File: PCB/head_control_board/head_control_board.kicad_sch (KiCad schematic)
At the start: 60 parts, among them Q1 AO3401A, U1 TPS63070RNMR, U2 TPS63070RNMR, U3 SN74AHCT245PWR, U4 ESP32-S3-WROOM-1(N16R8)

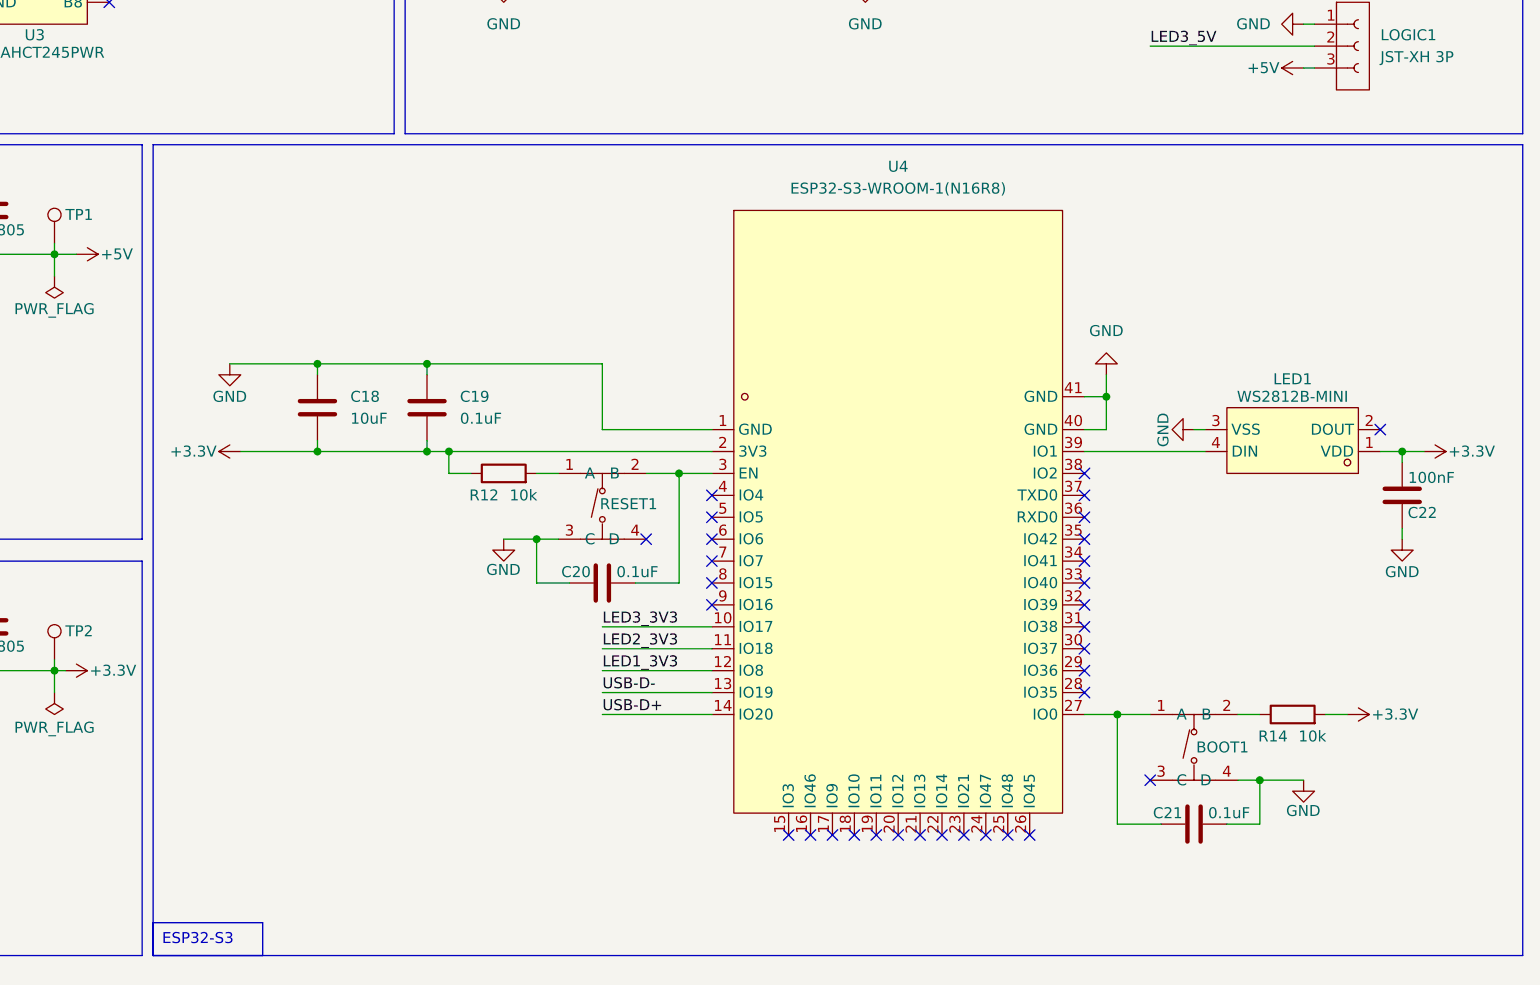
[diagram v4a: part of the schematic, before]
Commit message: Finish signal routing
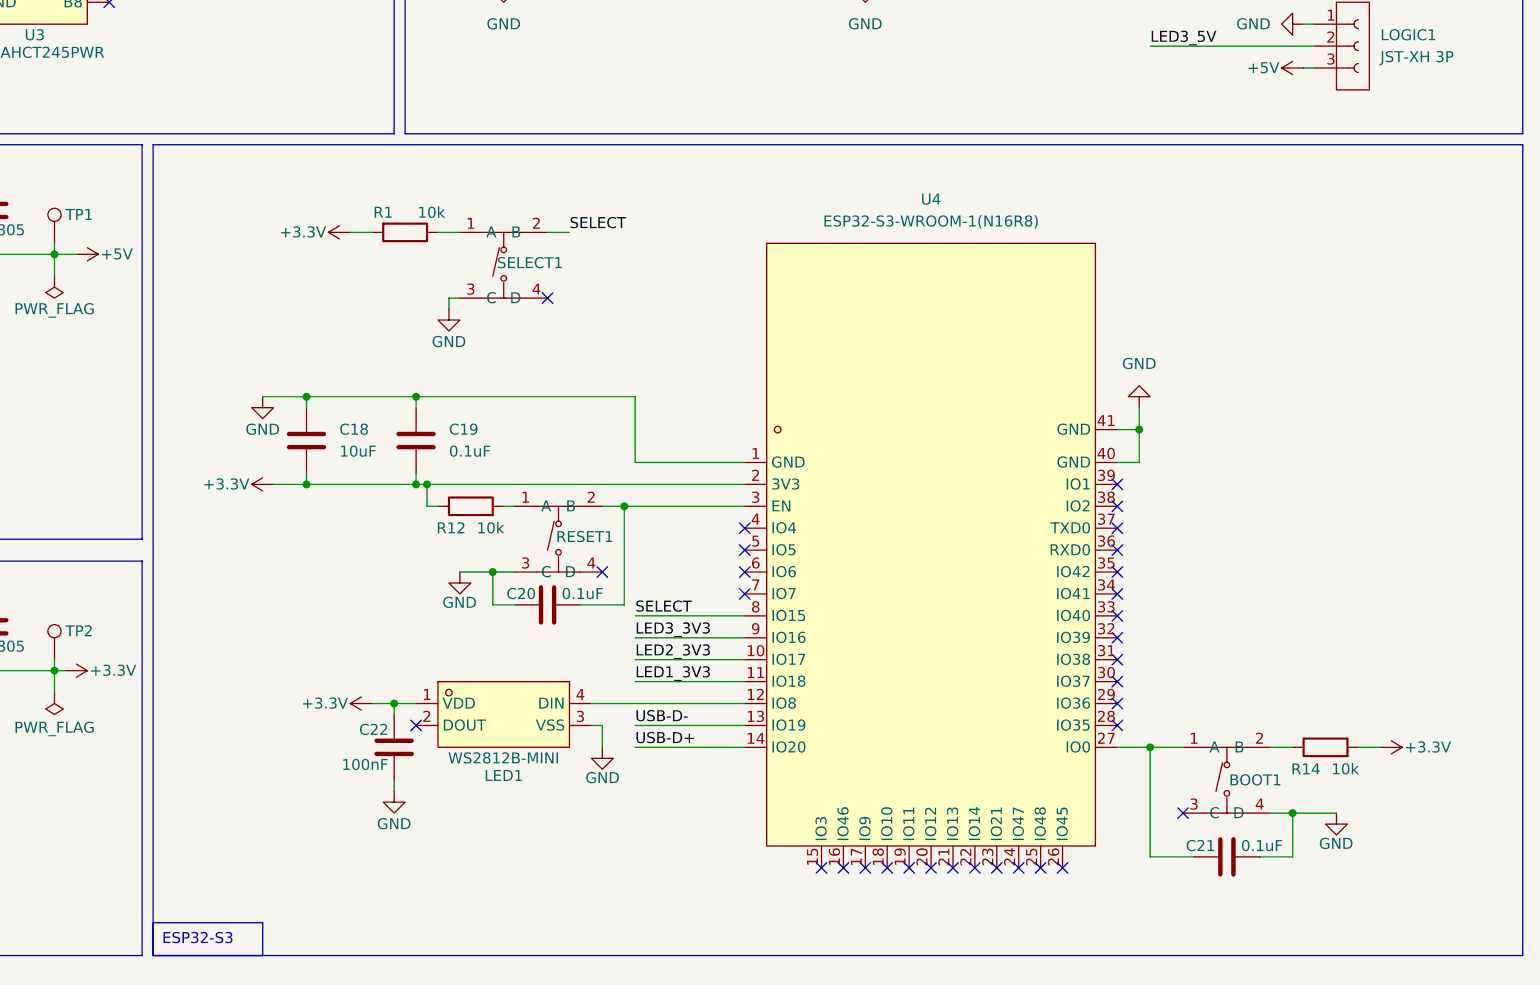
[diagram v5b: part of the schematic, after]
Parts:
- added R1: 10k, Resistor_SMD:R_0805_2012Metric, symbol Device:R
- added SELECT1: TS-1187A-B-A-B, LCSC:SW-SMD_4P-L5.1-W5.1-P3.70-LS6.5-TL-2, symbol LCSC:TS-1187A-B-A-B
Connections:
- net +3.3V: now also C22.1, R1.2; no longer C22.2
- net GND: now also C22.2, SELECT1.3 (C); no longer C22.1
- net LED1_3V3: now also U4.11 (IO18); no longer U4.12 (IO8)
- net LED2_3V3: now also U4.10 (IO17); no longer U4.11 (IO18)
- net LED3_3V3: now also U4.9 (IO16); no longer U4.10 (IO17)
- net at LED1.4 (DIN): now also U4.12 (IO8); no longer U4.39 (IO1)
- net SELECT: now reaches U4.8 (IO15)
- net SELECT: now also SELECT1.2 (B)
- new net: R1.1, SELECT1.1 (A)
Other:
- moved on the sheet: BOOT1, C18, C19, C20, C21, C22, LED1, R12, R14, RESET1, U4

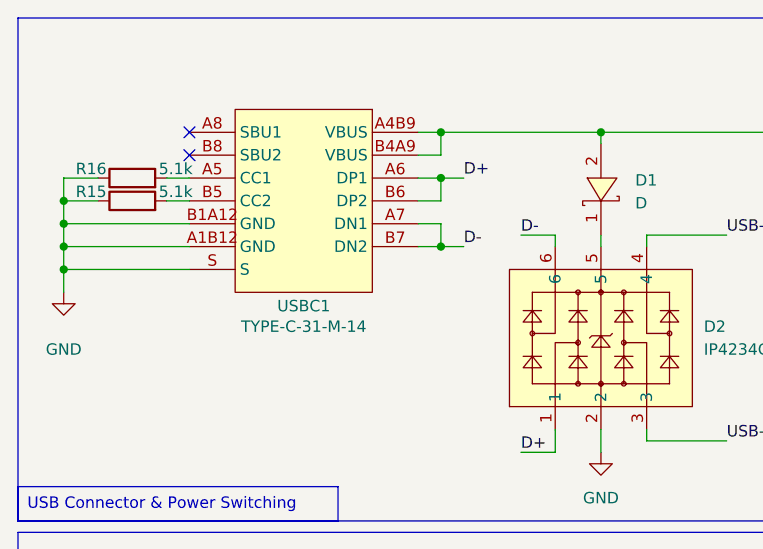
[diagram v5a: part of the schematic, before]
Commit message: Finish power routing
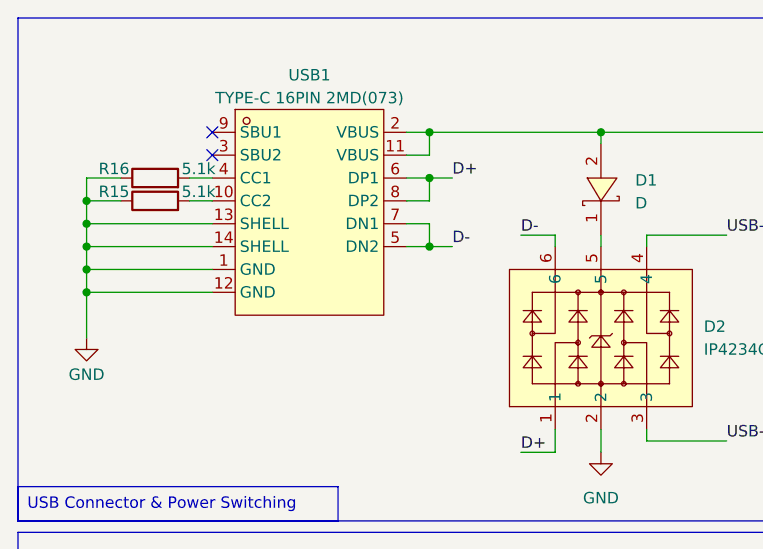
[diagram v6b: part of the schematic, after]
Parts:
- removed USBC1: TYPE-C-31-M-14, LCSC:USB-C-SMD_12P-P0.50-H-F_TYPE-C-31-M-14, symbol LCSC:TYPE-C-31-M-14
- added USB1: TYPE-C 16PIN 2MD(073), LCSC:USB-C-SMD_TYPE-C-6PIN-2MD-073, symbol LCSC:TYPE-C16PIN2MD(073)
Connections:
- net D+: now also USB1.6 (DP1), USB1.8 (DP2)
- net D-: now also USB1.5 (DN2), USB1.7 (DN1)
- net GND: now also USB1.1 (GND), USB1.12 (GND), USB1.13 (SHELL), USB1.14 (SHELL)
- net at D1.2, D3.2, Q1.1 (G)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: now also USB1.11 (VBUS), USB1.2 (VBUS)
- net at R15.2: now also USB1.10 (CC2)
- net at R16.2: now also USB1.4 (CC1)
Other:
- moved on the sheet: R15, R16

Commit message: Finish GND planes
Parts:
- COIL1, RADAR1: footprint Connector_JST:JST_XH_S2B-XH-A-1_1x02_P2.50mm_Horizontal -> jmatt:JST_XH_S2B-XH-A-1_1x02_P2.50mm_Horizontal
- HOLO1, LOGIC1, PSI1: footprint Connector_JST:JST_XH_S3B-XH-A-1_1x03_P2.50mm_Horizontal -> jmatt:JST_XH_S3B-XH-A-1_1x03_P2.50mm_Horizontal
- TP1, TP2, TP3: now left out of the parts list
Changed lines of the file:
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@@
 		(unit 1)
 		(exclude_from_sim no)
-		(in_bom yes)
+		(in_bom no)
 		(on_board yes)
 		(dnp no)
@@
 		(unit 1)
 		(exclude_from_sim no)
-		(in_bom yes)
+		(in_bom no)
 		(on_board yes)
 		(dnp no)
@@
 			)
 		)
-		(property "Footprint" "Connector_JST:JST_XH_S3B-XH-A-1_1x03_P2.50mm_Horizontal"
+		(property "Footprint" "jmatt:JST_XH_S3B-XH-A-1_1x03_P2.50mm_Horizontal"
 			(at 321.31 59.69 0)
 			(effects
@@
 		(unit 1)
 		(exclude_from_sim no)
-		(in_bom yes)
+		(in_bom no)
 		(on_board yes)
 		(dnp no)
@@
 			)
 		)
-		(property "Footprint" "Connector_JST:JST_XH_S2B-XH-A-1_1x02_P2.50mm_Horizontal"
+		(property "Footprint" "jmatt:JST_XH_S2B-XH-A-1_1x02_P2.50mm_Horizontal"
 			(at 240.03 30.48 0)
 			(effects
@@
 			)
 		)
-		(property "Footprint" "Connector_JST:JST_XH_S3B-XH-A-1_1x03_P2.50mm_Horizontal"
+		(property "Footprint" "jmatt:JST_XH_S3B-XH-A-1_1x03_P2.50mm_Horizontal"
 			(at 321.31 41.91 0)
 			(effects
@@
 			)
 		)
-		(property "Footprint" "Connector_JST:JST_XH_S3B-XH-A-1_1x03_P2.50mm_Horizontal"
+		(property "Footprint" "jmatt:JST_XH_S3B-XH-A-1_1x03_P2.50mm_Horizontal"
 			(at 321.31 24.13 0)
 			(effects
@@
 			)
 		)
-		(property "Footprint" "Connector_JST:JST_XH_S2B-XH-A-1_1x02_P2.50mm_Horizontal"
+		(property "Footprint" "jmatt:JST_XH_S2B-XH-A-1_1x02_P2.50mm_Horizontal"
 			(at 281.94 31.75 0)
 			(effects

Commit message: Start passive component selection
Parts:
- C1, C18, C2, C3, C4: LCSC Part (none) -> C440198
- C10, C22, C9: LCSC Part (none) -> C307331
- C11, C12, C13, C14, C15, C16: LCSC Part (none) -> C45783
- C17: value 10uF -> 0.1uF; LCSC Part (none) -> C49678
- C19, C20, C21: LCSC Part (none) -> C14663
- C5, C6, C7, C8: LCSC Part (none) -> C96446
- L1, L2: LCSC Part (none) -> C408444
- R1, R12, R14: LCSC Part (none) -> C17414
- R10, R11: LCSC Part (none) -> C60491
- R13: LCSC Part (none) -> C865587
- R15, R16: LCSC Part (none) -> C115337
- R3, R4: LCSC Part (none) -> C25744
- R5: LCSC Part (none) -> C149504
- R6: LCSC Part (none) -> C163456
- R7: LCSC Part (none) -> C25790
- R8: LCSC Part (none) -> C93946
- R9: LCSC Part (none) -> C25755
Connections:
- net GND: now also U3.5 (A4), U3.6 (A5), U3.7 (A6), U3.8 (A7), U3.9 (A8)
- no-connect marks 44 -> 39
